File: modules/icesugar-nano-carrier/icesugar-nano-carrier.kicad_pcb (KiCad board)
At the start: 2 copper layers, 24 x 45.7 mm, 4 parts, among them J1 Conn_01x06_Pin, J2 Conn_01x06_Pin, J3 Conn_02x06_Odd_Even

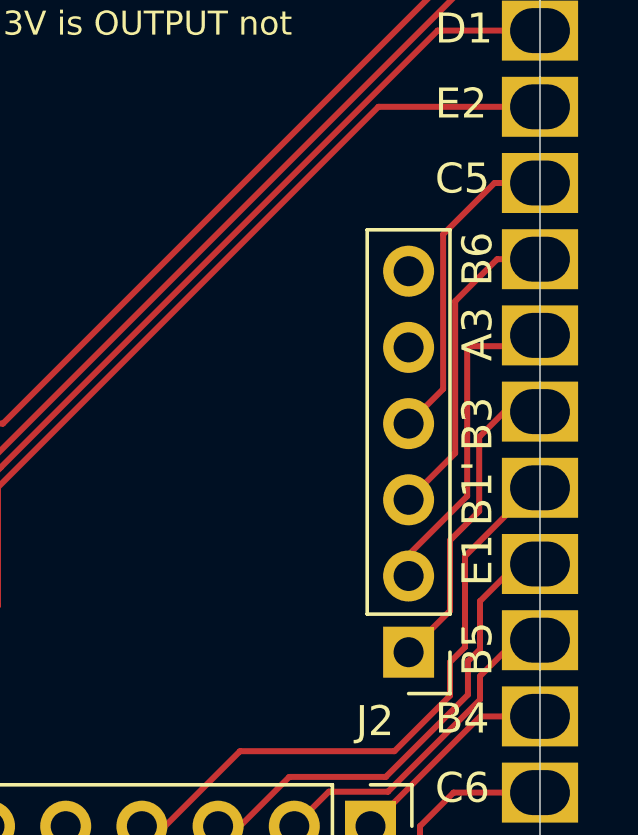
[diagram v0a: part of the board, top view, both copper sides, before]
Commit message: fix icesugar nano carrier pinout
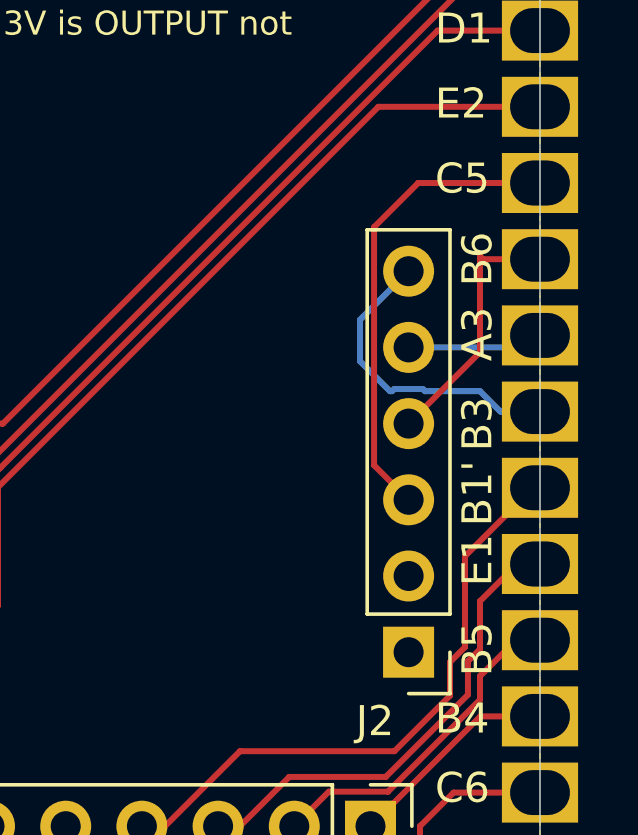
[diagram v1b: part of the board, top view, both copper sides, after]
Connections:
- J2 pad 1: B3 -> +3.3V
- J2 pad 2: A3 -> GND
- J2 pad 3: B6 -> C5
- J2 pad 4: C5 -> B6
- J2 pad 5: GND -> A3
- J2 pad 6: +3.3V -> B3
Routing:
- net A3: track 11.0 -> 4.55 mm
- net C5: track 10.7 -> 15.7 mm
- net B6: track 10.7 -> 8.61 mm
- net B3: track 10.5 -> 11.6 mm
- net GND: track 3.00 -> 3.71 mm
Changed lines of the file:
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@@
 			(layers "*.Cu" "*.Mask")
 			(remove_unused_layers no)
-			(net 9 "B3")
+			(net 4 "+3.3V")
 			(pinfunction "Pin_1")
 			(pintype "passive")
@@
 			(layers "*.Cu" "*.Mask")
 			(remove_unused_layers no)
-			(net 8 "A3")
+			(net 2 "GND")
 			(pinfunction "Pin_2")
 			(pintype "passive")
@@
 			(layers "*.Cu" "*.Mask")
 			(remove_unused_layers no)
-			(net 7 "B6")
+			(net 10 "C5")
 			(pinfunction "Pin_3")
 			(pintype "passive")
@@
 			(layers "*.Cu" "*.Mask")
 			(remove_unused_layers no)
-			(net 10 "C5")
+			(net 7 "B6")
 			(pinfunction "Pin_4")
 			(pintype "passive")
@@
 			(layers "*.Cu" "*.Mask")
 			(remove_unused_layers no)
-			(net 2 "GND")
+			(net 8 "A3")
 			(pinfunction "Pin_5")
 			(pintype "passive")
@@
 			(layers "*.Cu" "*.Mask")
 			(remove_unused_layers no)
-			(net 4 "+3.3V")
+			(net 9 "B3")
 			(pinfunction "Pin_6")
 			(pintype "passive")
@@
 	)
 	(segment
+		(start 7.62 10.16)
+		(end 7.62 9.453)
+		(width 0.2)
+		(layer "F.Cu")
+		(net 2)
+	)
+	(segment
 		(start -12 25)
 		(end -9 25)
@@
 	)
 	(segment
-		(start 9.172 6.068)
-		(end 9.172 1)
+		(start 10 2.7)
+		(end 7.62 5.08)
 		(width 0.2)
 		(layer "F.Cu")
@@
 	)
 	(segment
-		(start 7.62 7.62)
-		(end 9.172 6.068)
+		(start 10.1 -0.4)
+		(end 10 -0.5)
 		(width 0.2)
 		(layer "F.Cu")
@@
 	)
 	(segment
-		(start 10.572 -0.4)
-		(end 12 -0.4)
+		(start 12 -0.4)
+		(end 10.1 -0.4)
 		(width 0.2)
 		(layer "F.Cu")
@@
 	)
 	(segment
-		(start 9.172 1)
-		(end 10.572 -0.4)
+		(start 10 -0.5)
+		(end 10 2.7)
 		(width 0.2)
 		(layer "F.Cu")
@@
 	)
 	(segment
-		(start 9.573 2.5)
-		(end 11.64 2.5)
-		(width 0.2)
-		(layer "F.Cu")
+		(start 7.62 2.54)
+		(end 11.6 2.54)
+		(width 0.2)
+		(layer "B.Cu")
 		(net 8)
 	)
 	(segment
-		(start 11.64 2.5)
+		(start 11.6 2.54)
 		(end 12 2.14)
 		(width 0.2)
-		(layer "F.Cu")
+		(layer "B.Cu")
 		(net 8)
-	)
-	(segment
-		(start 7.62 9.453)
-		(end 9.573 7.5)
-		(width 0.2)
-		(layer "F.Cu")
-		(net 8)
-	)
-	(segment
-		(start 9.573 7.5)
-		(end 9.573 2.5)
-		(width 0.2)
-		(layer "F.Cu")
-		(net 8)
-	)
-	(segment
-		(start 7.62 10.16)
-		(end 7.62 9.453)
-		(width 0.2)
-		(layer "F.Cu")
-		(net 8)
-	)
-	(segment
-		(start 9 11.32)
-		(end 9 8.974)
-		(width 0.2)
-		(layer "F.Cu")
-		(net 9)
 	)
 	(segment
@@
 	)
 	(segment
-		(start 9.974 5.526)
-		(end 10.82 4.68)
-		(width 0.2)
-		(layer "F.Cu")
+		(start 8.16776 4)
+		(end 8.09676 3.929)
+		(width 0.2)
+		(layer "B.Cu")
 		(net 9)
 	)
 	(segment
-		(start 7.62 12.7)
-		(end 9 11.32)
-		(width 0.2)
-		(layer "F.Cu")
+		(start 7 4)
+		(end 6 3)
+		(width 0.2)
+		(layer "B.Cu")
 		(net 9)
 	)
 	(segment
-		(start 9 8.974)
-		(end 9.974 8)
-		(width 0.2)
-		(layer "F.Cu")
+		(start 7.07224 4)
+		(end 7 4)
+		(width 0.2)
+		(layer "B.Cu")
 		(net 9)
 	)
 	(segment
-		(start 9.974 8)
-		(end 9.974 5.526)
-		(width 0.2)
-		(layer "F.Cu")
+		(start 7.14324 3.929)
+		(end 7.07224 4)
+		(width 0.2)
+		(layer "B.Cu")
 		(net 9)
 	)
 	(segment
-		(start 8.771 3.929)
-		(end 8.771 -1.229)
+		(start 10.68 4.68)
+		(end 10 4)
+		(width 0.2)
+		(layer "B.Cu")
+		(net 9)
+	)
+	(segment
+		(start 10 4)
+		(end 8.16776 4)
+		(width 0.2)
+		(layer "B.Cu")
+		(net 9)
+	)
+	(segment
+		(start 8.09676 3.929)
+		(end 7.14324 3.929)
+		(width 0.2)
+		(layer "B.Cu")
+		(net 9)
+	)
+	(segment
+		(start 6 3)
+		(end 6 1.62)
+		(width 0.2)
+		(layer "B.Cu")
+		(net 9)
+	)
+	(segment
+		(start 12 4.68)
+		(end 10.68 4.68)
+		(width 0.2)
+		(layer "B.Cu")
+		(net 9)
+	)
+	(segment
+		(start 6 1.62)
+		(end 7.62 0)
+		(width 0.2)
+		(layer "B.Cu")
+		(net 9)
+	)
+	(segment
+		(start 6.469 6.469)
+		(end 7.62 7.62)
 		(width 0.2)
 		(layer "F.Cu")
@@
 	)
 	(segment
-		(start 8.771 -1.229)
-		(end 10.482 -2.94)
+		(start 6.469 -1.469)
+		(end 6.469 6.469)
 		(width 0.2)
 		(layer "F.Cu")
@@
 	)
 	(segment
-		(start 7.62 5.08)
-		(end 8.771 3.929)
+		(start 12 -2.94)
+		(end 7.94 -2.94)
 		(width 0.2)
 		(layer "F.Cu")
@@
 	)
 	(segment
-		(start 10.482 -2.94)
-		(end 12 -2.94)
-		(width 0.2)
-		(layer "F.Cu")
+		(start 7.94 -2.94)
+		(end 6.469 -1.469)
+		(width 0.2)
+		(layer "F.Cu")
